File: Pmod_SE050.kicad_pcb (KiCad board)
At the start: 2 copper layers, 21.1 x 21.6 mm, 8 parts, among them IC1 SE050C1HQ1_Z01SCZ, J1 Conn_02x03_Odd_Even, J2 Conn_01x06, J3 Conn_01x06

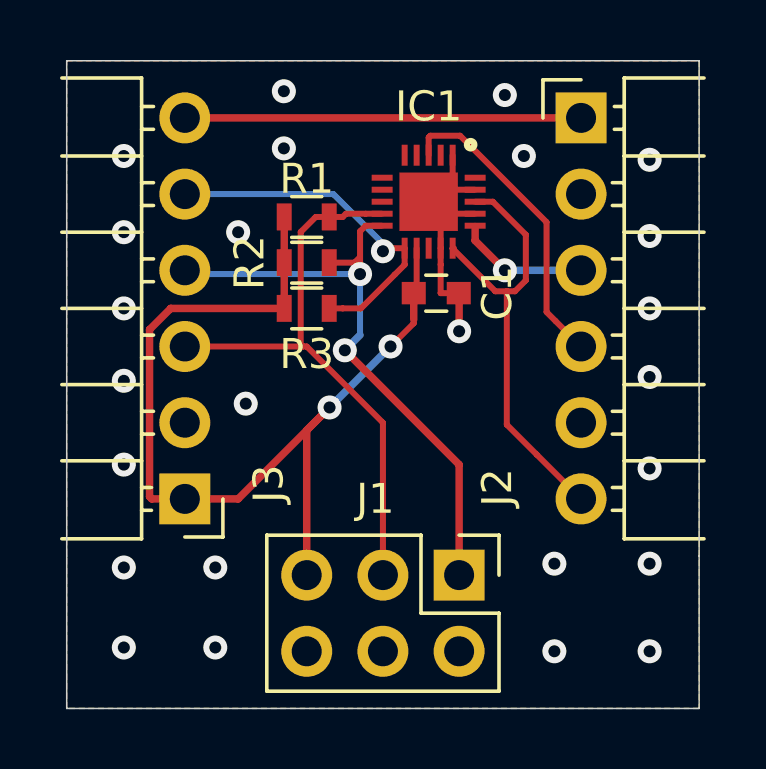
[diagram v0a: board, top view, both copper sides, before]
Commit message: Rev 2.0 of the board
New version of the breakout board.
Schematic is the same but the board is smaller.
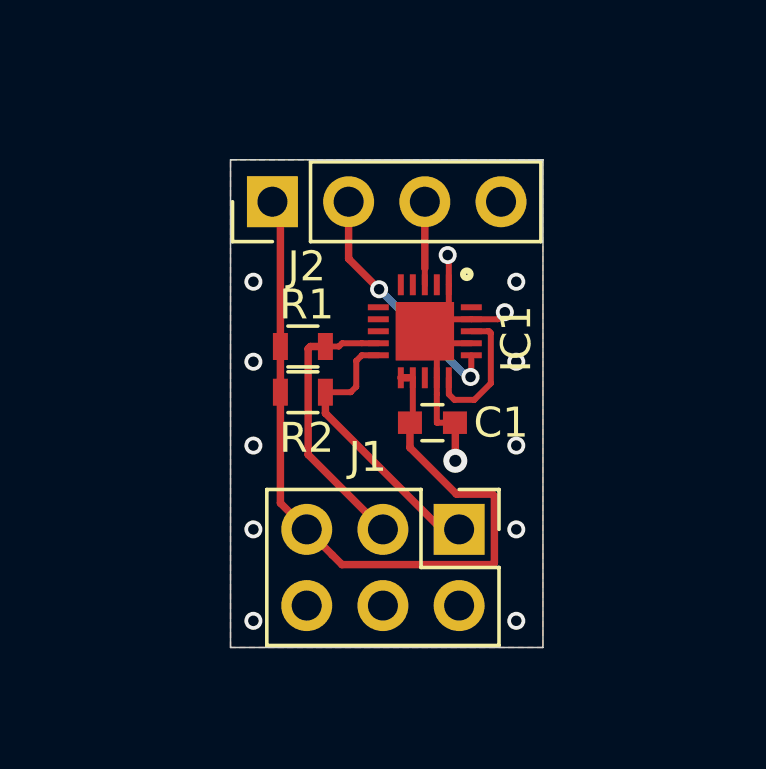
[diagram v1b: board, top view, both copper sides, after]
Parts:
- removed J3: Conn_01x06, Pmod_SE050:PinHeader_1x06_P2.54mm_Horizontal
- removed R3: 10k, Pmod_SE050:R_0603
- J2: value Conn_01x06 -> Conn_01x04; footprint Pmod_SE050:PinHeader_1x06_P2.54mm_Horizontal -> Connector_PinHeader_2.54mm:PinHeader_1x04_P2.54mm_Vertical
- moved J2 10.7 mm to (130.2, 63.8), turned to 90 degrees
- moved IC1 4.32 mm to (135.3, 68.1)
- moved C1 4.32 mm to (135.5, 71.1)
- moved R1 4.32 mm to (131.2, 68.6)
- moved R2 4.32 mm to (131.2, 70.1)
- moved J1 1.52 mm to (136.4, 74.7)
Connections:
- IC1 pad 11: /ENA -> +3V3
- J2 pad 1: /INT -> +3V3
- J2 pad 2: Net-(J2-Pad2) -> /TRUSTED_SCL
- J2 pad 3: /TRUSTED_SCL -> /TRUSTED_SDA
- J2 pad 4: /TRUSTED_SDA -> GND
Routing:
- net /INT: track 13.5 -> 0.00 mm
- net /SCL: track 21.8 -> 9.56 mm, vias 2 -> 0
- net /ENA: track 12.2 -> 0.00 mm, vias 1 -> 0
- net /SDA: track 19.8 -> 9.47 mm
- net /VOUT: track 14.8 -> 4.61 mm
- net /TRUSTED_SDA: track 10.4 -> 2.77 mm
- net +3V3: track 33.1 -> 27.0 mm, vias 2 -> 0
- net /TRUSTED_SCL: track 4.41 -> 8.33 mm, vias 1 -> 2
- net GND: track 9.84 -> 12.1 mm, vias 25 -> 13
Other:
- board size 21.1 x 21.6 mm -> 10.4 x 16.3 mm
- board text added: "SE050 v2.0 OTS Security"
- board text added: "TSCL"
- board text added: "TSDA"
- board text removed: "ENA"
- board text removed: "IO0"
- board text removed: "N.C."
- board text removed: "SE050 Ext. board v1.0"
- board text removed: "Tscl"
- board text removed: "Tsda"
